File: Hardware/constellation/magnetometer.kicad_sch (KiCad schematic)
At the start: 1 part, among them U5 MMC5883MA

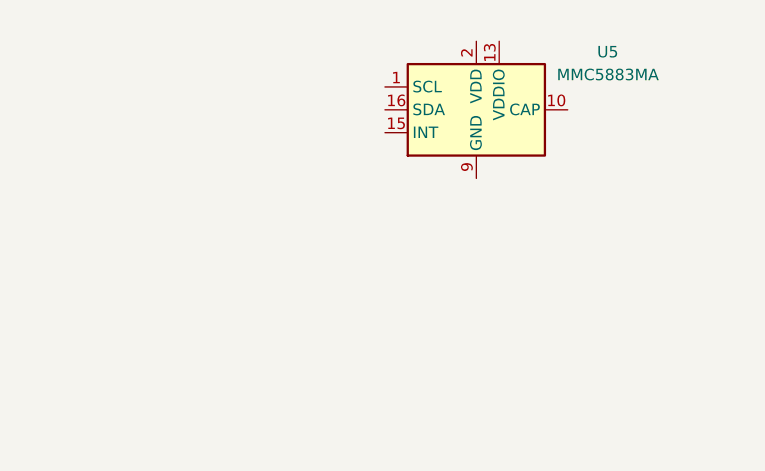
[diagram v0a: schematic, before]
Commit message: shift to hierarchial design, add GNSS, mag, accel
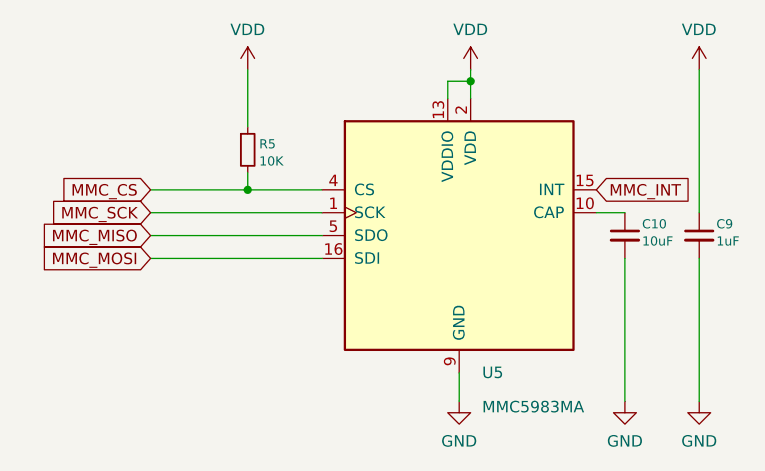
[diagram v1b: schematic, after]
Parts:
- added C10: 10uF, Capacitor_SMD:C_0402_1005Metric, symbol Device:C_Small
- added C9: 1uF, Capacitor_SMD:C_0402_1005Metric, symbol Device:C_Small
- added R5: 10K, Resistor_SMD:R_0402_1005Metric_Pad0.72x0.64mm_HandSolder, symbol Device:R_Small
- U5: value MMC5883MA -> MMC5983MA
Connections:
- net MMC_SCK: now reaches U5.1 (SCK)
- net at U5.10 (CAP): now also C10.1
- net GND: now reaches U5.11 (GND), U5.9 (GND)
- net GND: now also C10.2, C9.2
- net VDD: now reaches U5.13 (VDDIO)
- net VDD: now also U5.2 (VDD), C9.1, R5.1
- net MMC_INT: now reaches U5.15 (INT)
- net MMC_MOSI: now reaches U5.16 (SDI)
- net MMC_CS: now reaches U5.4 (CS)
- net MMC_CS: now also R5.2
- net MMC_MISO: now reaches U5.5 (SDO)
